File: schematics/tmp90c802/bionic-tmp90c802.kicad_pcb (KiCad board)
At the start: 2 copper layers, 27.9 x 68.6 mm, 8 parts, among them J1 Bionic-P135, J2 Bionic-P245, U1 TMP90C802A, U2 11AA010-I/TT

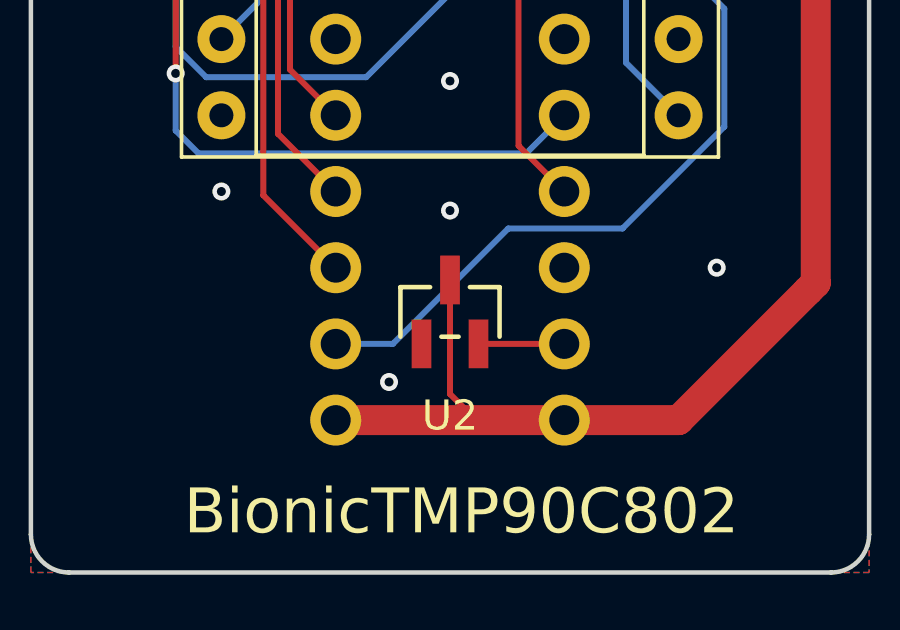
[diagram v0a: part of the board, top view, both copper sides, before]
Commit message: [TMP90C802] Fix EEPROM pinout
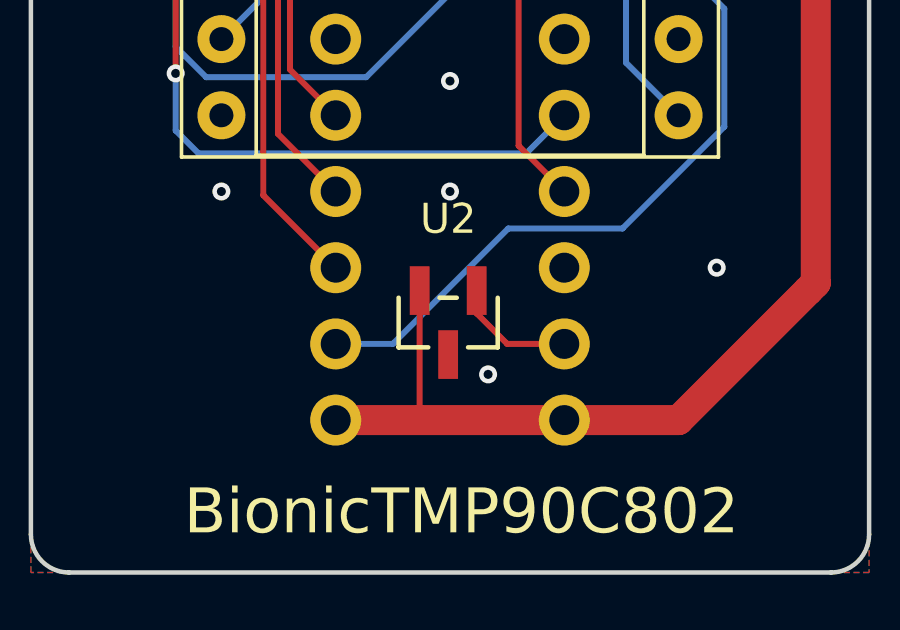
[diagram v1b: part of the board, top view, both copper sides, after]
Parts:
- J1: footprint connector:Bionic-P135_Vertical -> 0-LocalLibrary:Bionic-P135_Vertical
- J2: footprint connector:Bionic-P245_Vertical -> 0-LocalLibrary:Bionic-P245_Vertical
- moved U2 0.36 mm to (114.9, 130.2), turned to 180 degrees
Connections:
- U2 pad 1: GND -> Net-(J2-P57)
- U2 pad 2: Net-(J2-P57) -> VCC
- U2 pad 3: VCC -> GND
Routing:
- net Net-(J2-P57): track 2.94 -> 4.10 mm
- net VCC: track 91.9 -> 91.0 mm
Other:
- board text added: "Rev. 6"
- board text removed: "Rev. 5"
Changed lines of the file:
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@@
   (title_block
     (title "BionicTMP90C802")
-    (date "2024-04-29")
-    (rev "5")
+    (date "2024-11-02")
+    (rev "6")
     (company "Tadashi G. Takaoka")
   )
@@
   )
   (footprint "0-LocalLibrary:SOT-23_MC_MCH-M" (layer "F.Cu")
-    (at 114.97 129.894)
+    (at 114.908999 130.248 180)
     (descr "Microchip 11AAxxx-I/TT UNI/O 1Kbit Serial EEPROM")
     (property "Sheetfile" "bionic-tmp90c802.kicad_sch")
@@
         (effects (font (size 1 1) (thickness 0.15)))
     )
-    (fp_text value "11AA010-I/TT" (at 0 0 unlocked) (layer "F.Fab")
+    (fp_text value "11AA010-I/TT" (at 0 0 180 unlocked) (layer "F.Fab")
         (effects (font (size 1 1) (thickness 0.15)))
     )
-    (fp_text user "${REFERENCE}" (at 0 0 unlocked) (layer "F.Fab")
+    (fp_text user "${REFERENCE}" (at 0 0 180 unlocked) (layer "F.Fab")
         (effects (font (size 1 1) (thickness 0.15)))
     )
@@
     (fp_circle (center -1.270999 0.446) (end -1.143999 0.446)
       (stroke (width 0.0254) (type solid)) (fill none) (layer "F.Fab"))
-    (pad "1" smd rect (at -0.950001 1.066) (size 0.6604 1.6256) (layers "F.Cu" "F.Paste" "F.Mask")
+    (pad "1" smd rect (at -0.950001 1.066 180) (size 0.6604 1.6256) (layers "F.Cu" "F.Paste" "F.Mask")
+      (net 42 "Net-(J2-P57)") (pinfunction "SCIO") (pintype "bidirectional"))
+    (pad "2" smd rect (at 0.950001 1.066 180) (size 0.6604 1.6256) (layers "F.Cu" "F.Paste" "F.Mask")
+      (net 1 "VCC") (pinfunction "VCC") (pintype "power_in"))
+    (pad "3" smd rect (at 0 -1.066 180) (size 0.6604 1.6256) (layers "F.Cu" "F.Paste" "F.Mask")
       (net 2 "GND") (pinfunction "VSS") (pintype "power_in"))
-    (pad "2" smd rect (at 0.950001 1.066) (size 0.6604 1.6256) (layers "F.Cu" "F.Paste" "F.Mask")
-      (net 42 "Net-(J2-P57)") (pinfunction "SCIO") (pintype "bidirectional"))
-    (pad "3" smd rect (at 0 -1.066) (size 0.6604 1.6256) (layers "F.Cu" "F.Paste" "F.Mask")
-      (net 1 "VCC") (pinfunction "VCC") (pintype "power_in"))
     (model "${KIPRJMOD}/0-LocalLibrary/SOT-23_MC_MCH.step"
       (offset (xyz 0 0 0))
@@
     )
   )
-  (footprint "connector:Bionic-P135_Vertical" locked (layer "B.Cu")
+  (footprint "0-LocalLibrary:Bionic-P135_Vertical" locked (layer "B.Cu")
     (at 111.16 75.08 180)
     (descr "Through hole straight pin header, 1x24, 2.54mm pitch, single row")
@@
     )
   )
-  (footprint "connector:Bionic-P245_Vertical" locked (layer "B.Cu")
+  (footprint "0-LocalLibrary:Bionic-P245_Vertical" locked (layer "B.Cu")
     (at 118.78 75.08 180)
     (descr "Through hole straight pin header, 1x24, 2.54mm pitch, single row")
@@
     (effects (font (size 0.8 0.8)) (justify bottom mirror))
   )
-  (gr_text "Rev. 5" (at 107.096 136.802) (layer "B.SilkS")
+  (gr_text "Rev. 6" (at 107.096 136.802) (layer "B.SilkS")
     (effects (font (size 1 1)) (justify left mirror))
   )
@@
   (segment (start 127.162 75.281) (end 126.961 75.08) (width 1) (layer "F.Cu") (net 1))
   (segment locked (start 125.13 75.08) (end 124.114 75.08) (width 1) (layer "F.Cu") (net 1))
-  (segment (start 114.97 132.6271) (end 115.8429 133.5) (width 0.2) (layer "F.Cu") (net 1))
   (segment (start 122.59 133.5) (end 126.908 129.182) (width 1) (layer "F.Cu") (net 1))
-  (segment locked (start 111.16 133.5) (end 118.78 133.5) (width 1) (layer "F.Cu") (net 1))
+  (segment (start 113.958998 133.495002) (end 113.954 133.5) (width 0.2) (layer "F.Cu") (net 1))
+  (segment (start 113.958998 129.182) (end 113.958998 133.495002) (width 0.2) (layer "F.Cu") (net 1))
   (segment (start 115.7447 71.778) (end 119.288 71.778) (width 0.2) (layer "F.Cu") (net 1))
+  (segment (start 113.954 133.5) (end 118.78 133.5) (width 1) (layer "F.Cu") (net 1))
+  (segment (start 111.16 133.5) (end 113.954 133.5) (width 1) (layer "F.Cu") (net 1))
   (segment (start 127.162 128.928) (end 127.162 75.281) (width 1) (layer "F.Cu") (net 1))
-  (segment (start 114.97 128.624) (end 114.97 132.6271) (width 0.2) (layer "F.Cu") (net 1))
   (segment locked (start 124.114 75.08) (end 122.59 75.08) (width 1) (layer "F.Cu") (net 1))
   (segment (start 125.13 74.9265) (end 125.13 75.08) (width 0.2) (layer "F.Cu") (net 1))
@@
   (via (at 123.86 128.42) (size 0.6) (drill 0.3) (layers "F.Cu" "B.Cu") (net 2))
   (via (at 114.97 115.72) (size 0.6) (drill 0.3) (layers "F.Cu" "B.Cu") (free) (net 2))
-  (via (at 114.97 126.515) (size 0.6) (drill 0.3) (layers "F.Cu" "B.Cu") (free) (net 2))
+  (via (at 114.97 125.88) (size 0.6) (drill 0.3) (layers "F.Cu" "B.Cu") (free) (net 2))
   (via (at 114.97 122.197) (size 0.6) (drill 0.3) (layers "F.Cu" "B.Cu") (free) (net 2))
-  (via (at 112.938 132.23) (size 0.6) (drill 0.3) (layers "F.Cu" "B.Cu") (net 2))
+  (via (at 116.24 131.976) (size 0.6) (drill 0.3) (layers "F.Cu" "B.Cu") (net 2))
   (segment (start 107.35 97.94) (end 102.27 97.94) (width 0.2) (layer "B.Cu") (net 2))
   (segment (start 111.16 130.96) (end 113.065 130.96) (width 0.2) (layer "B.Cu") (net 3))
@@
   (segment (start 109.636 88.122346) (end 110.563654 89.05) (width 0.2) (layer "B.Cu") (net 38))
   (segment (start 113.7 100.48) (end 118.78 100.48) (width 0.2) (layer "B.Cu") (net 38))
-  (segment (start 116.124 130.96) (end 115.92 130.756) (width 0.2) (layer "F.Cu") (net 42))
-  (segment (start 118.78 130.96) (end 116.124 130.96) (width 0.2) (layer "F.Cu") (net 42))
+  (segment (start 115.859 129.182) (end 115.859 129.944) (width 0.2) (layer "F.Cu") (net 42))
+  (segment (start 115.859 129.944) (end 116.875 130.96) (width 0.2) (layer "F.Cu") (net 42))
+  (segment (start 116.875 130.96) (end 118.78 130.96) (width 0.2) (layer "F.Cu") (net 42))
   (segment (start 111.668 94.13) (end 112.684 95.146) (width 0.2) (layer "F.Cu") (net 45))
   (segment (start 109.636 91.59) (end 109.636 93.241) (width 0.2) (layer "F.Cu") (net 45))

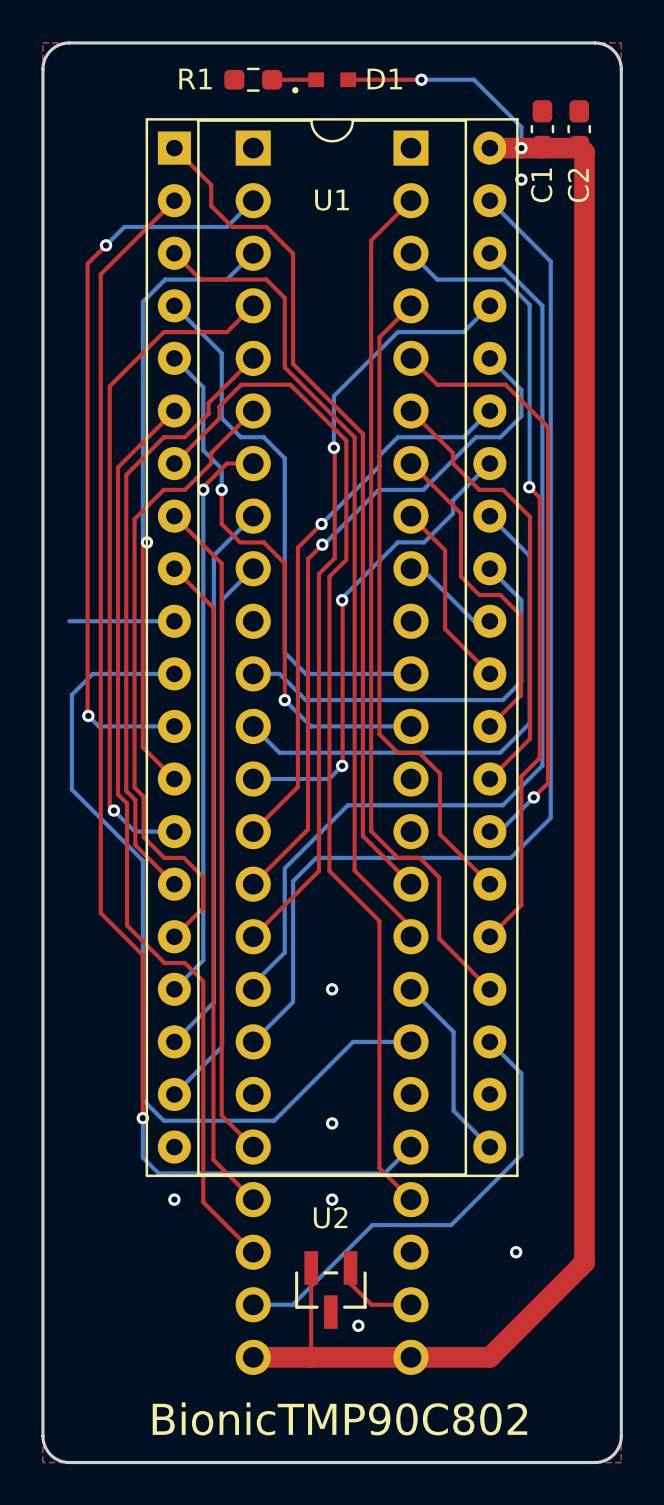
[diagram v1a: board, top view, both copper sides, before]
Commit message: [TMP90C802] Shrink board size
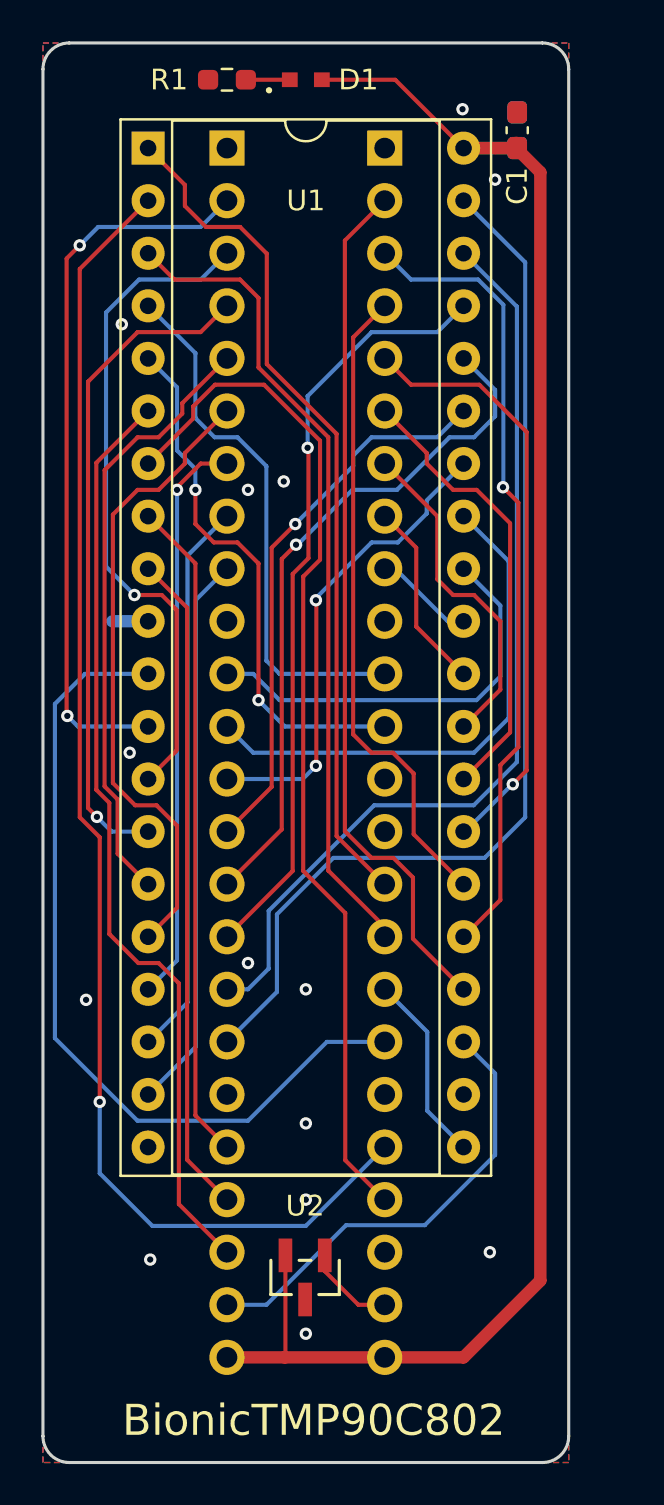
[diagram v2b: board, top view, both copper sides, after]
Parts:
- C2: moved to B.Cu
- moved C2 3.00 mm to (123.9, 74.2)
- moved U2 1.39 mm to (113.7, 129.6)
- moved D1 1.27 mm to (113.7, 71.8)
- moved J1 1.27 mm to (109.9, 75.1)
- moved J2 1.27 mm to (117.5, 75.1)
- moved R1 1.27 mm to (109.9, 71.8)
- moved U1 1.27 mm to (106.1, 75.1)
- moved C1 1.22 mm to (123.9, 74.2)
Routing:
- net GND: track 5.08 -> 1.73 mm, vias 7 -> 14
- net /P54: track 62.3 -> 65.2 mm
- net /P11: track 30.2 -> 32.3 mm
- net /P37: track 53.3 -> 52.1 mm
- net /P36: track 46.8 -> 45.8 mm
- net /P47: track 41.3 -> 40.4 mm
- net VCC: track 91.0 -> 90.3 mm, vias 2 -> 0
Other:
- board size 27.9 x 68.6 mm -> 25.4 x 68.6 mm

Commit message: [TMP90C802] Fix INT0/INT1 footprints
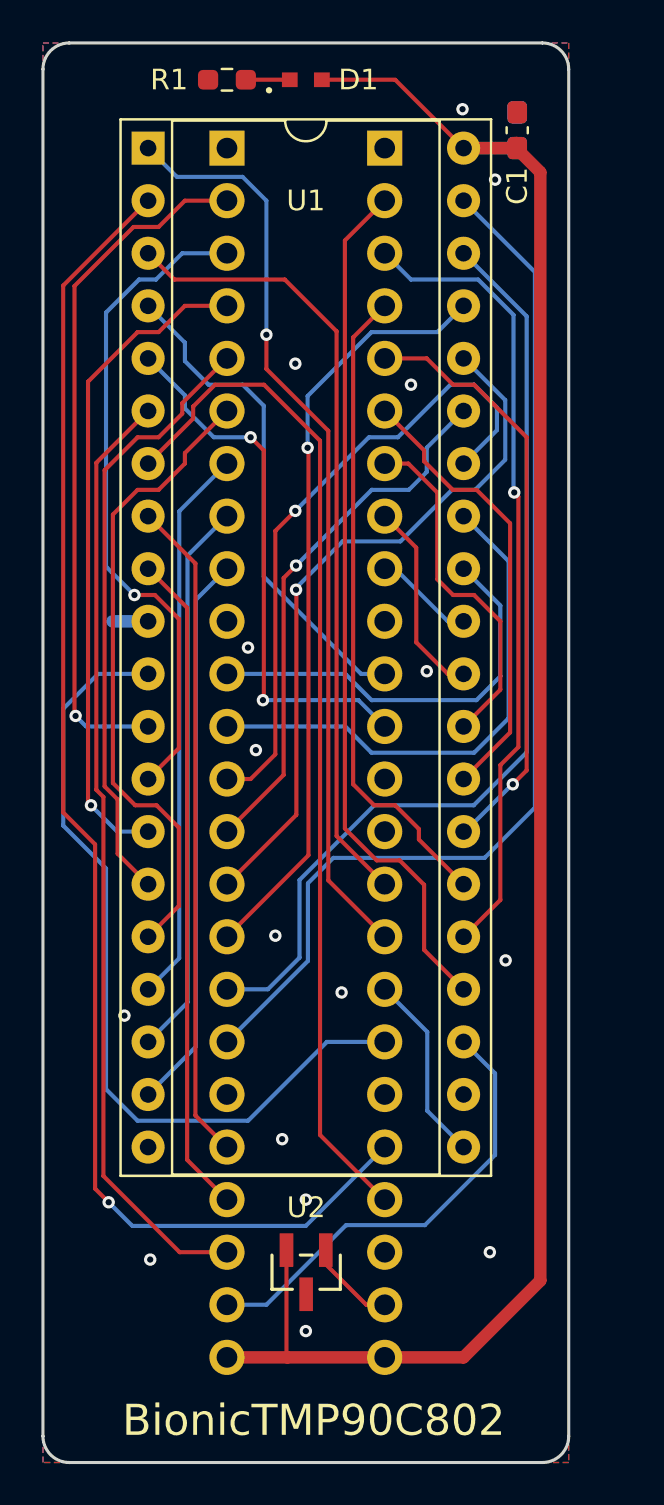
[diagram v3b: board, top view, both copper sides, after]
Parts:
- moved U2 0.26 mm to (113.7, 129.4)
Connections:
- U1 pad 1: /P44 -> /P45
- U1 pad 3: /P45 -> /P44
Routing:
- net /P32: track 22.9 -> 31.1 mm, vias 2 -> 1
- net /P45: track 39.6 -> 44.7 mm, vias 0 -> 1
- net /P44: track 41.3 -> 38.3 mm
- net /P40: track 26.1 -> 24.2 mm
- net /P10: track 35.1 -> 33.6 mm, vias 2 -> 1
- net /P54: track 65.2 -> 66.4 mm
- net /P36: track 45.8 -> 46.8 mm
- net /P33: track 26.9 -> 26.1 mm
- net /P52: track 44.9 -> 45.6 mm
- net /P15: track 27.7 -> 27.0 mm, vias 1 -> 0
- net /P34: track 33.4 -> 34.1 mm
- net /P47: track 40.4 -> 39.7 mm
- net /P55: track 50.0 -> 49.3 mm
- net /P25: track 16.3 -> 17.0 mm
- net GND: vias 14 -> 16
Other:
- board text added: "Rev. 7"
- board text removed: "Rev. 6"

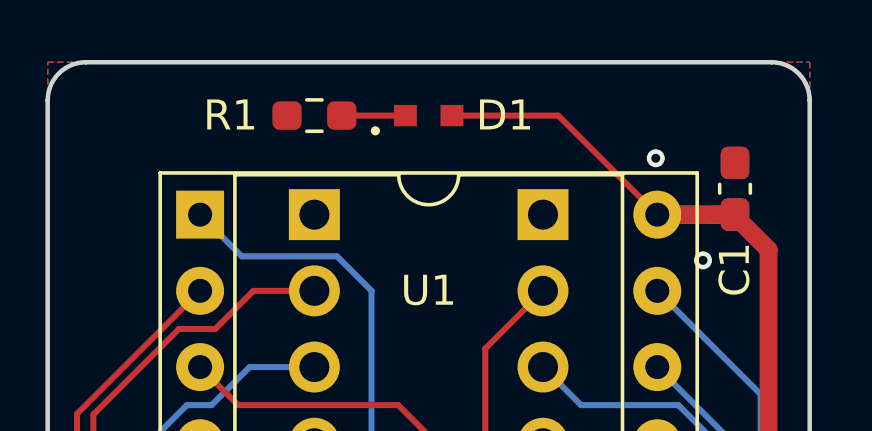
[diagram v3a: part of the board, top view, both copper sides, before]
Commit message: [schematics] Update LED footprint
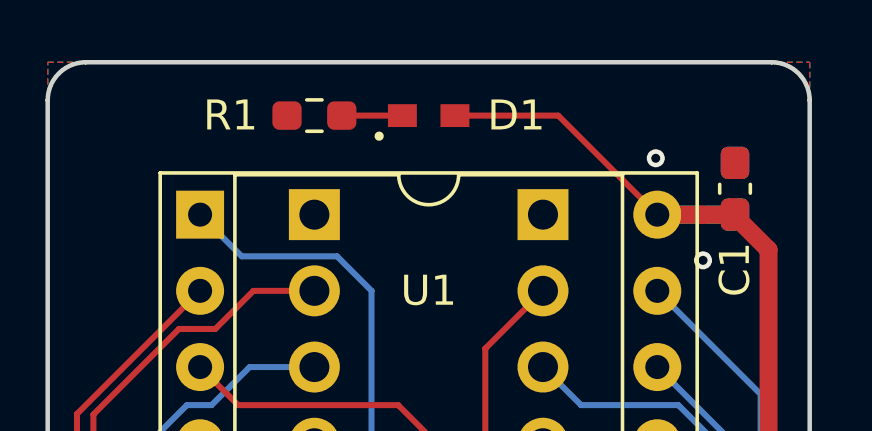
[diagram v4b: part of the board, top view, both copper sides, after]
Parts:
- D1: footprint 0-LocalLibrary:LED_CSL1901UW1_ROM -> 0-LocalLibrary:LED_CSL1901UW1_ROM-M
